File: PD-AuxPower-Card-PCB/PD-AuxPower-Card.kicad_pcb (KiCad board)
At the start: 4 copper layers, 76 x 41 mm, 119 parts, among them J1 1.27mm 1x4P, J2 1.27mm 1x4P, J3 USB_C_Receptacle_USB2.0, J4 2.54mm terminal, J5 2.54mm terminal, Q1 FDMC86520L, Q2 FDMC86520L, SW1 TSA017A2510A, SW2 K3-1296S-E1, SW3 K3-1296S-E1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

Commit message: Initial commit. Add source file of PCB and Firmware, the firmware not support any communication yet, but only can show LED effect for its alive.
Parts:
- R10, R11, R12, R13: value 499 -> 2k
- R5: value 1k -> 2k
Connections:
- U3 pad 3: +3V3 -> VBUS
- U4 pad 1: I2C1_SDA -> I2C1_SCL
- U4 pad 3: I2C1_SCL -> I2C1_SDA
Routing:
- net +3V3: track 85.3 -> 80.5 mm, vias 17 -> 16
- net GND: track 55.3 -> 51.1 mm
- net I2C1_SCL: track 33.1 -> 29.2 mm
- net I2C1_SDA: track 25.6 -> 26.5 mm
- net VBUS: track 14.3 -> 14.8 mm

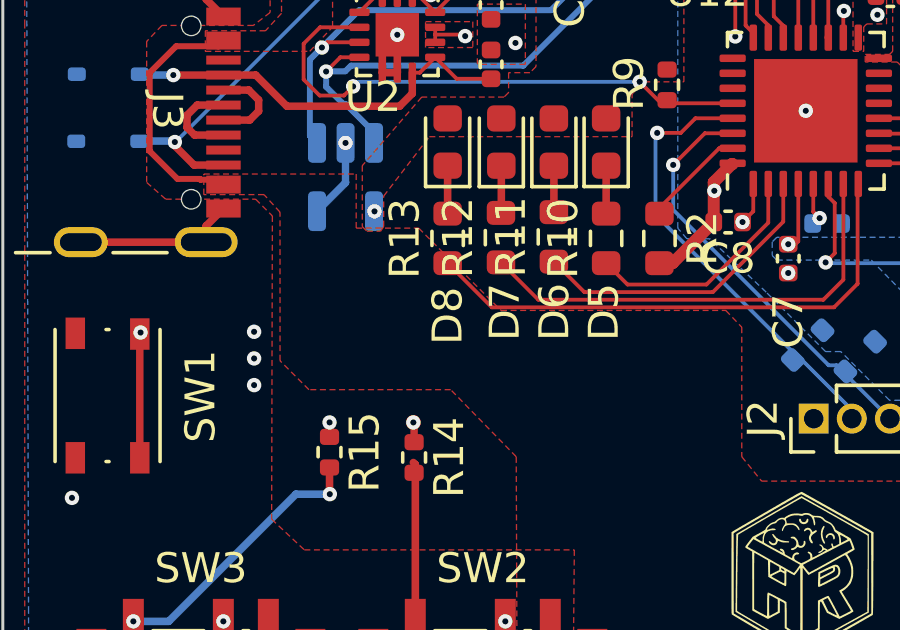
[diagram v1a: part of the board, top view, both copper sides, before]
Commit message: FEAT: Add PID algorithm for output voltage control. NOT TUNE YET! Change ADC1 trigger source into TIM1 TRGO for update event. Synchronised TIM2 and TIM1 by using slave mode. PCB: Change TL431 to TLV431 for 3.3V output rail. Change some tuned resistor value for next sample.
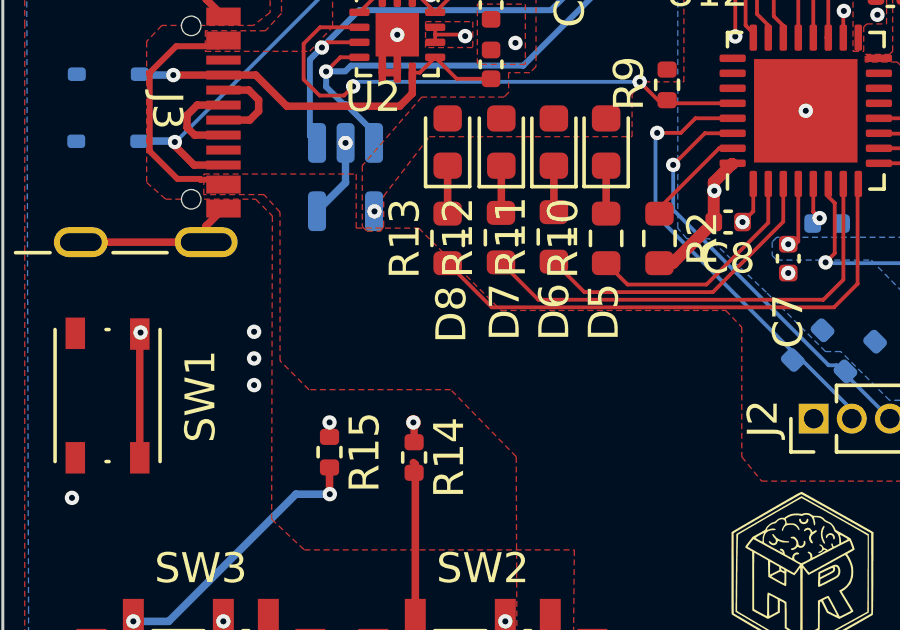
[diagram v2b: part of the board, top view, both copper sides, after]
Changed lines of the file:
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@@
     (property "ki_keywords" "LED diode")
     (attr smd)
-    (fp_text reference "D8" (at -5.7913 0 90) (layer "F.SilkS")
+    (fp_text reference "D8" (at -5.7405 0.127 90) (layer "F.SilkS")
         (effects (font (size 1 1) (thickness 0.153)))
     )

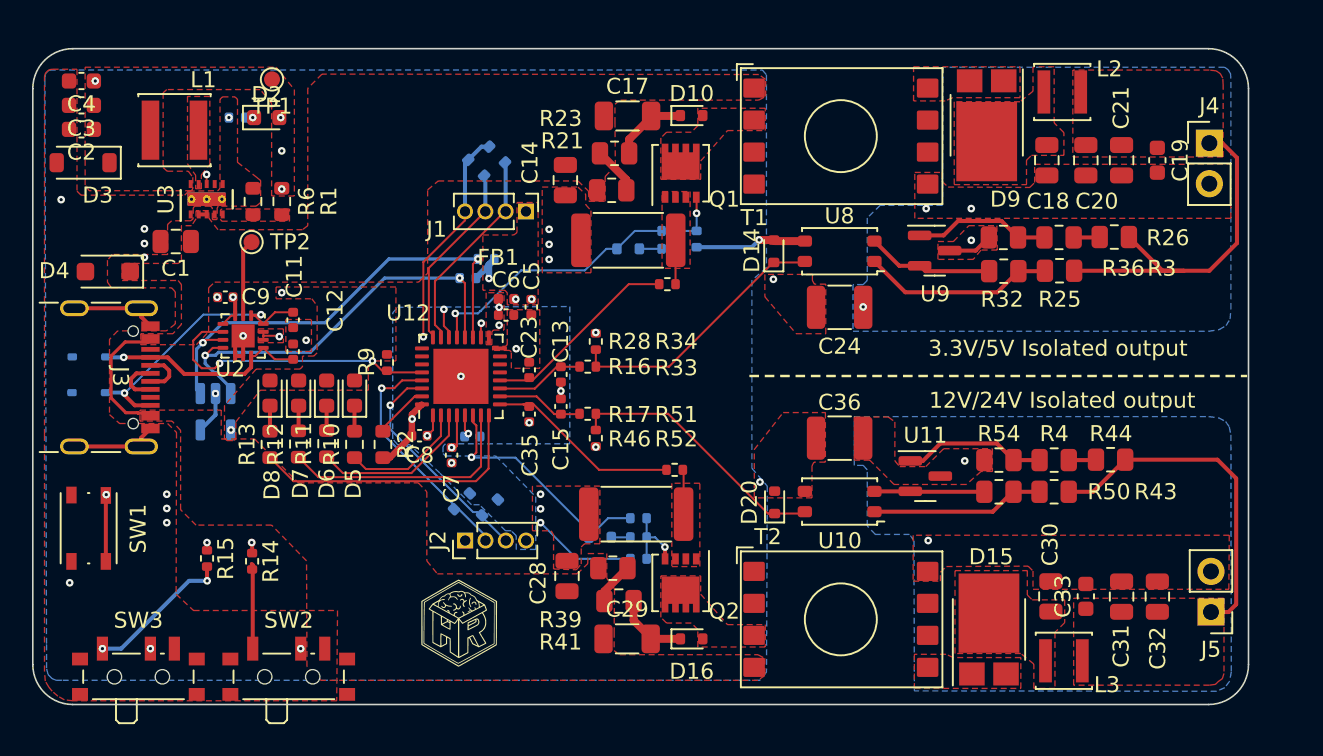
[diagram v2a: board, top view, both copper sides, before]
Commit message: PCB: Update LTV-214 footprint and update to PCB layout.
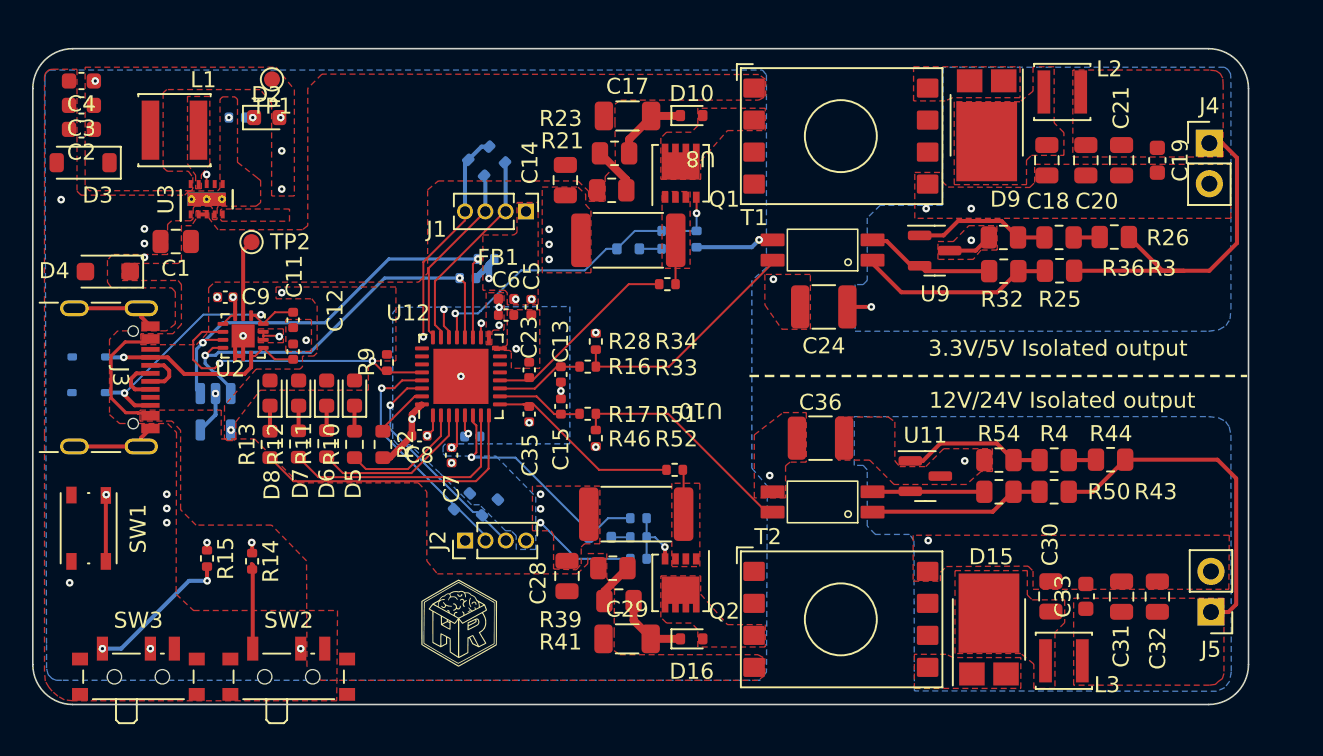
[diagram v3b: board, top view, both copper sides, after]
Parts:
- removed D14, D20: MM5Z3V3, Diode_SMD:D_SOD-523
- removed R1: 160k, Resistor_SMD:R_0603_1608Metric
- removed R6: 51k, Resistor_SMD:R_0603_1608Metric
- R2: value 499 -> 1k
- R25: value 360 -> 110
- R26: value 10k -> 8.2k
- R28, R46: value 10k -> 50
- R43: value 360 -> 1.2k
- R44: value 48k -> 33k
- T1, T2: value EFD10 -> ER 9.5
- U10, U8: value EL3H7(C)(TA)-G -> LTV-217; footprint OptoDevice:Panasonic_APV-AQY_SSOP-4_4.45x2.65mm_P1.27mm -> Library:SOP-4-175mil
- U9: value TL431DBZ -> TLV431BFTA
- moved C36 1.19 mm to (118.7, 103.6)
- moved U8 1.07 mm to (118.9, 91.8)
- moved U10 1.07 mm to (118.9, 107.6)
- moved C24 0.99 mm to (119.0, 95.4)
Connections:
- U3 pad 5: Net-(U3-FB) -> GND
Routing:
- net Net-(R16-Pad2): track 16.9 -> 14.9 mm
- net Net-(R17-Pad2): track 16.7 -> 14.8 mm
- net GND: track 51.1 -> 49.3 mm
- net GND1: track 2.79 -> 4.28 mm
- removed copper zone on F.Cu, net Net-(U3-FB)

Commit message: FEAT: Revolution PCB to ver 1.0. Change COMP1+ to 3v3 current sense, COMP2+ to 12V current sense and 12V LED to GPIO7 output. Modify PCB layout.
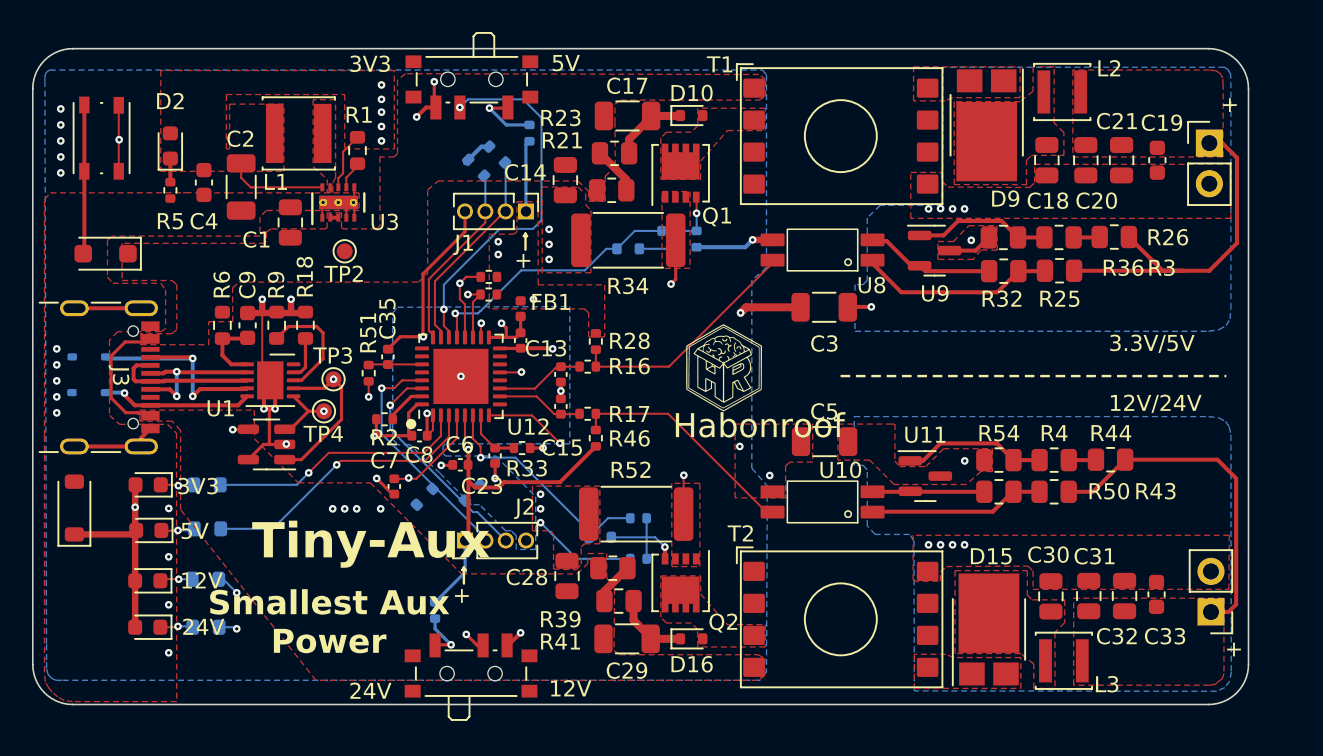
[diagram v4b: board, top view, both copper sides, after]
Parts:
- removed C11, C12: 330p, Capacitor_SMD:C_0402_1005Metric
- removed C24, C36: 1n/500V, Capacitor_SMD:C_1210_3225Metric
- removed R29, R47: 10, Resistor_SMD:R_0402_1005Metric
- removed TP1: TestPoint, TestPoint:TestPoint_Pad_D1.0mm
- removed U2: FUSB302BMPX, Package_DFN_QFN:WQFN-14-1EP_2.5x2.5mm_P0.5mm_EP1.45x1.45mm
- added R1: 100k, Resistor_SMD:R_0603_1608Metric, F.Cu at (89.8, 85.6)
- added R18: 10k, Resistor_SMD:R_0603_1608Metric, F.Cu at (86.5, 96.5)
- added R6: 10, Resistor_SMD:R_0603_1608Metric, F.Cu at (81.4, 96.5)
- added TP3: SCL, TestPoint:TestPoint_Pad_D1.0mm, F.Cu at (88.3, 99.9)
- added TP4: SDA, TestPoint:TestPoint_Pad_D1.0mm, F.Cu at (87.7, 101.9)
- added U1: HUSB328_DD2, Package_DFN_QFN:DFN-10-1EP_3x3mm_P0.5mm_EP1.65x2.38mm, F.Cu at (84.3, 100.0)
- C1: value 10uF/50V -> 2.2u/35V
- C10, R7, R8, U4: moved to F.Cu
- C2: value 10u/6.3V -> 22u/10V; footprint Capacitor_SMD:C_0603_1608Metric -> Capacitor_SMD:C_1206_3216Metric
- C3: value 10u/6.3V -> 2200p/500V; footprint Capacitor_SMD:C_0603_1608Metric -> Capacitor_SMD:C_1206_3216Metric
- C5: value 0.1u -> 2200p/500V; footprint Capacitor_SMD:C_0402_1005Metric -> Capacitor_SMD:C_1206_3216Metric
- C9: value 0.1u -> 1u; footprint Capacitor_SMD:C_0402_1005Metric -> Capacitor_SMD:C_0603_1608Metric
- J1: value 1.27mm 1x4P -> SWD
- J2: value 1.27mm 1x4P -> UART
- R10, R11, R12, R13: value 2k -> 10k; moved to B.Cu
- R14, R15: value 1k -> 10k; moved to B.Cu
- R2: value 1k -> 10k; footprint Resistor_SMD:R_0603_1608Metric -> Resistor_SMD:R_0402_1005Metric
- R25: value 110 -> 1k
- R26: value 8.2k -> 0
- R3: value 0 -> 8.2k
- R43: value 1.2k -> 6.8k
- R5: value 2k -> 10k; moved to F.Cu
- R9: value 4.7k -> 10k; footprint Resistor_SMD:R_0402_1005Metric -> Resistor_SMD:R_0603_1608Metric
- T1, T2: footprint User:Transformer_ER9.5_11.6mmx8.2mm -> Johnson's:Transformer_ER9.5_11.6mmx8.2mm
- TP2: value TestPoint -> VIN
- moved C3 48.1 mm to (119.0, 95.4), turned to 0 degrees
- moved SW3 42.2 mm to (97.0, 81.5), turned to 180 degrees
- moved R15 33.4 mm to (100.5, 84.5), turned to 90 degrees
- moved SW1 24.4 mm to (73.8, 84.8)
- moved G*** 23.0 mm to (112.7, 99.1)
- moved D3 21.6 mm to (72.1, 108.0), turned to 90 degrees
- moved C5 20.2 mm to (119.0, 103.8), turned to 0 degrees
- moved R51 20.1 mm to (90.5, 99.5), turned to -90 degrees
- moved D8 16.5 mm to (76.7, 115.4), turned to 180 degrees
- moved D7 15.1 mm to (76.7, 112.5), turned to 180 degrees
- moved D5 14.1 mm to (76.7, 106.5), turned to 180 degrees
- moved D6 14.0 mm to (76.8, 109.3), turned to 180 degrees
- moved R33 13.7 mm to (100.1, 104.2)
- moved R13 12.1 mm to (80.3, 115.4), turned to 180 degrees
- moved R14 11.8 mm to (94.7, 114.3)
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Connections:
- C10 pad 1: Net-(U12-VDDA) -> Net-(C10-Pad1)
- C3 pad 1: +3V3 -> GND
- C3 pad 2: GND -> GND1
- C5 pad 1: +3V3 -> GND
- C5 pad 2: GND -> GND2
- C6 pad 1: Net-(U12-VDDA) -> +3V3
- C8 pad 1: Net-(U12-VDDA) -> Net-(C10-Pad1)
- C9 pad 1: +3V3 -> Net-(U1-VIN)
- FB1 pad 1: +3V3 -> Net-(C10-Pad1)
- FB1 pad 2: Net-(U12-VDDA) -> +3V3
- Q1 pad 4: Net-(Q1-G) -> Net-(D12-A)
- Q2 pad 4: Net-(Q2-G) -> Net-(D18-A)
- R24 pad 1: Net-(Q1-G) -> Net-(D12-A)
- R30 pad 2: Net-(Q1-G) -> Net-(D12-A)
- R42 pad 1: Net-(Q2-G) -> Net-(D18-A)
- R48 pad 2: Net-(Q2-G) -> Net-(D18-A)
- R7 pad 2: I2C1_SCL -> I2C1_SDA
- R8 pad 2: I2C1_SDA -> I2C1_SCL
- R9 pad 1: +3V3 -> Net-(U1-VSET)
- R9 pad 2: USB_INT -> GND
- U12 pad 1: Net-(U12-VDDA) -> Net-(C10-Pad1)
- U12 pad 12: Iout1_fb -> unconnected-(U12-PA6-Pad12)
- U12 pad 13: unconnected-(U12-PA7-Pad13) -> LED_12v
- U12 pad 17: Net-(U12-VDDA) -> Net-(C10-Pad1)
- U12 pad 27: unconnected-(U12-PB4-Pad27) -> Iout2_fb
- U12 pad 28: USB_INT -> unconnected-(U12-PB5-Pad28)
- U12 pad 5: Net-(U12-VDDA) -> +3V3
- U12 pad 7: LED_12v -> Iout1_fb
- U12 pad 9: Iout2_fb -> unconnected-(U12-PA3-Pad9)
- U3 pad 7: unconnected-(U3-PG-Pad7) -> Net-(U3-PG)
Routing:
- net GND: track 49.3 -> 90.4 mm, vias 29 -> 44
- net NRST: track 29.2 -> 59.0 mm
- net LED_12v: track 15.4 -> 44.5 mm, vias 0 -> 2
- net Vout1_sel: track 49.5 -> 25.5 mm
- net Net-(Q2-S): track 2.76 -> 25.1 mm, vias 0 -> 2
- net LED_24v: track 17.9 -> 37.9 mm, vias 0 -> 2
- net Net-(Q1-S): track 2.75 -> 21.2 mm, vias 0 -> 2
- net USB_INT: track 18.3 -> 0.00 mm, vias 2 -> 0
- net Net-(C10-Pad1): track 0.00 -> 17.2 mm, vias 0 -> 2
- net Vout2_sel: track 40.3 -> 23.4 mm
- net Iout2_fb: track 12.5 -> 3.34 mm
- net Iout1_fb: track 12.4 -> 3.59 mm
- net LED_3v3: track 7.85 -> 16.3 mm, vias 0 -> 1
- net Net-(D21-A1): track 17.3 -> 9.23 mm, vias 2 -> 1
- net LED_5v: track 10.3 -> 18.0 mm, vias 0 -> 1
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- removed copper zone on F.Cu, net Net-(U12-VDDA)
- removed copper zone on In1.Cu, net Net-(U12-VDDA)
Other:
- board text added: "+"
- board text added: "12V"
- board text added: "12V/24V"
- board text added: "24V"
- board text added: "3.3V/5V"
- board text added: "3V3"
- board text added: "5V"
- board text added: "Habonroof"
- board text added: "Smallest Aux Power"
- board text added: "Tiny-Aux"
- board text removed: "12V/24V Isolated output"
- board text removed: "3.3V/5V Isolated output"
